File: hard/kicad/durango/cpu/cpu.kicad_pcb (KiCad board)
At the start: 2 copper layers, 34 parts, among them J1 NANOLINK, J2 IO9 INPUT, J3 IO8 PORT, Q1 BC547, Q2 BC547, Q3 BC547, SW1 RESET, U1 65SC02, U10 4040, U11 74HC30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

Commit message: routing in the Mac
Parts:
- moved D1 67.5 mm to (94.0, 78.7)
- moved U8 66.5 mm to (168.9, 121.9), turned to 180 degrees
- moved U6 61.3 mm to (147.3, 104.1)
- moved U10 30.7 mm to (189.2, 104.1)
- moved U11 30.7 mm to (175.3, 106.7)
- moved BZ1 24.3 mm to (188.0, 61.0)
- moved D3 19.9 mm to (182.9, 71.1), turned to 90 degrees
- moved R5 19.3 mm to (186.7, 71.1), turned to 90 degrees
- moved U5 19.1 mm to (193.7, 74.9)
- moved Q3 18.2 mm to (188.0, 49.5), turned to 270 degrees
- moved R4 15.5 mm to (200.7, 62.2), turned to 90 degrees
- moved R3 7.41 mm to (129.5, 116.8), turned to 270 degrees
- moved U4 6.35 mm to (180.3, 74.9)
- moved D2 3.81 mm to (200.7, 49.5), turned to 270 degrees
- moved D4 2.84 mm to (182.9, 59.7), turned to 90 degrees
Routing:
- net /DI7: track 5.08 -> 41.3 mm
- net /DI6: track 5.08 -> 37.8 mm
- net /D4: track 54.8 -> 86.4 mm, vias 2 -> 3
- net /D5: track 74.4 -> 105.2 mm, vias 6 -> 7
- net /D6: track 52.8 -> 82.9 mm, vias 3 -> 4
- net /DI5: track 5.08 -> 34.2 mm
- net /DI0: track 5.08 -> 32.4 mm, vias 0 -> 1
- net /DI1: track 5.08 -> 30.6 mm, vias 0 -> 1
- net /DI4: track 5.08 -> 30.6 mm
- net /DI2: track 5.08 -> 28.8 mm, vias 0 -> 1
- net /IEN: track 0.00 -> 22.6 mm
- net /DI3: track 5.08 -> 27.0 mm, vias 0 -> 1
- net GND: track 11.4 -> 23.4 mm, vias 0 -> 1
- net Net-(C1-Pad1): track 0.00 -> 8.67 mm
- net +5V: track 37.9 -> 45.5 mm

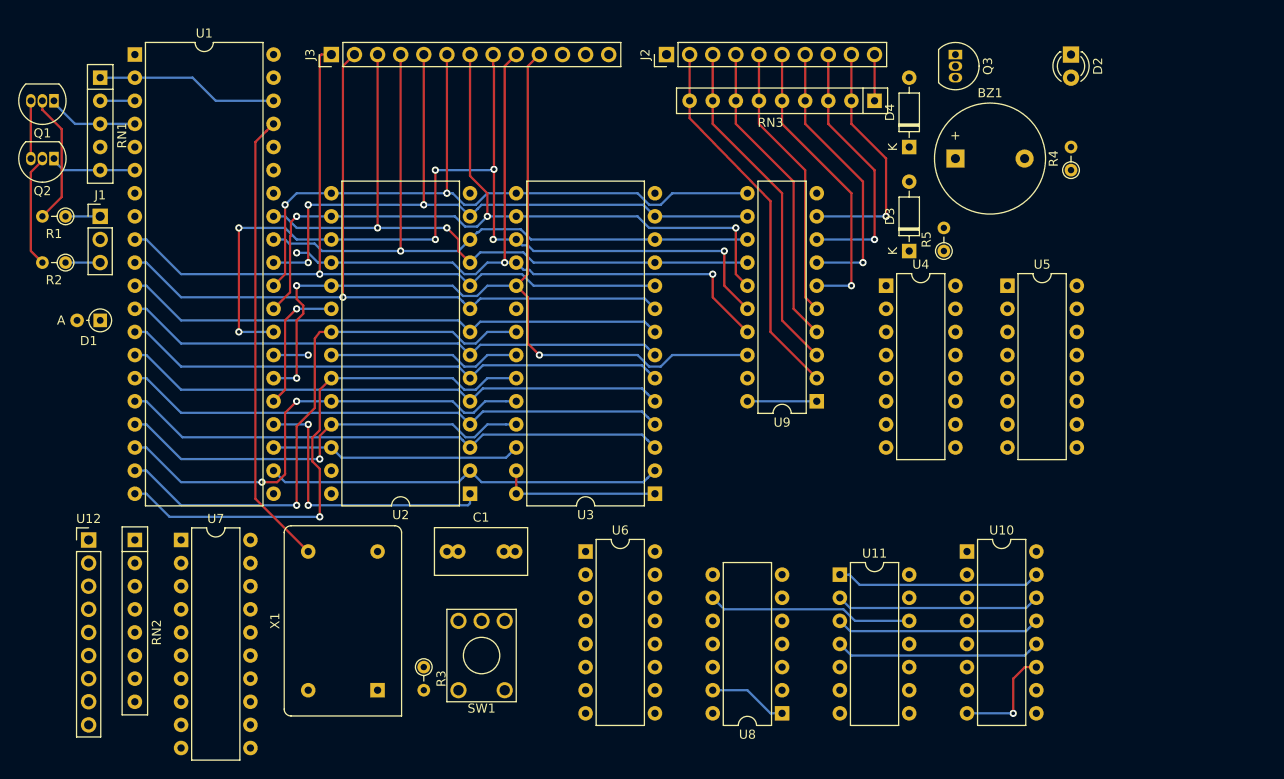
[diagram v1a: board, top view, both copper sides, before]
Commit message: more routing in Raspberry Pi
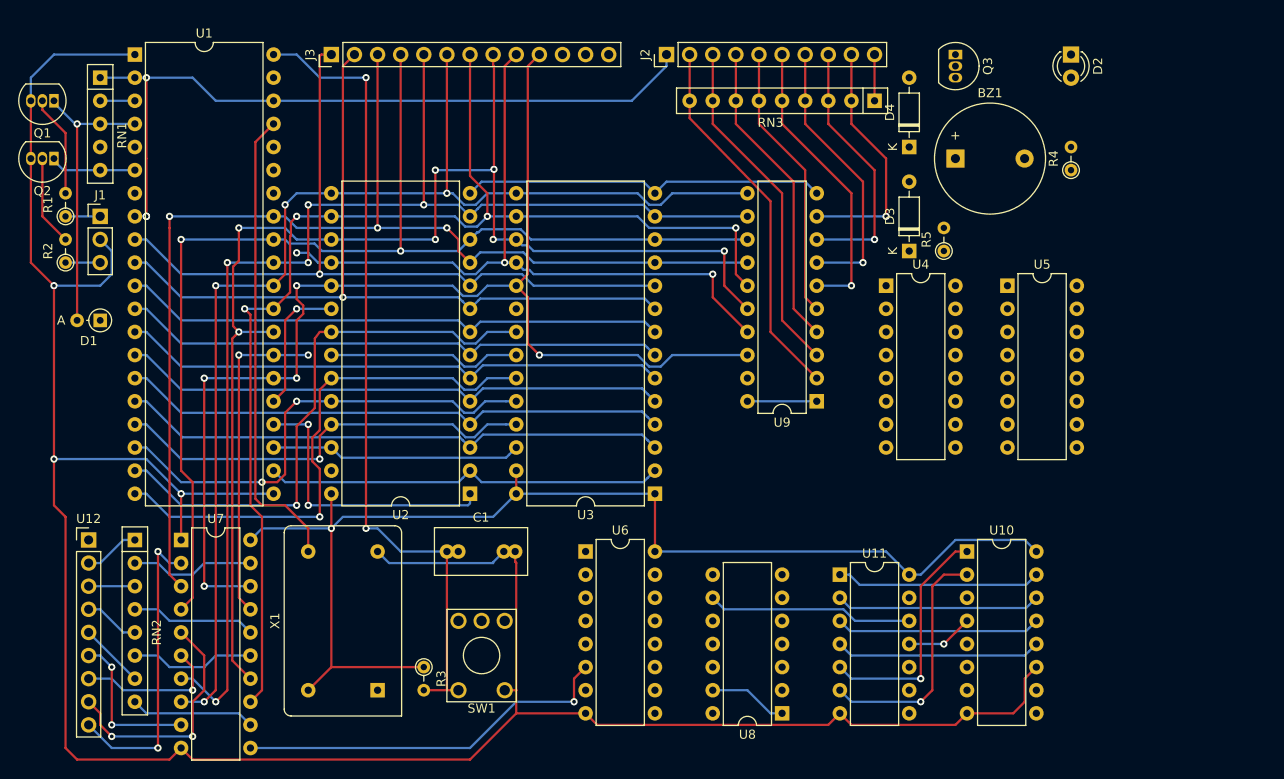
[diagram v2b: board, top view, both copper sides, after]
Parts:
- turned R1 to 90 degrees
- turned R2 to 90 degrees
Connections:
- U11 pad 14: (no net) -> +5V
- U11 pad 7: (no net) -> GND
- U4 pad 16: (no net) -> +5V
- U4 pad 8: (no net) -> GND
- U5 pad 16: (no net) -> +5V
- U5 pad 8: (no net) -> GND
- U6 pad 16: (no net) -> +5V
- U6 pad 8: (no net) -> GND
- U8 pad 14: (no net) -> +5V
- U8 pad 7: (no net) -> GND
- X1 pad 7: Net-(U1-Pad39) -> GND
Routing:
- net GND: track 23.4 -> 325.1 mm, vias 1 -> 3
- net +5V: track 45.5 -> 223.6 mm, vias 0 -> 4
- net Net-(C1-Pad1): track 8.67 -> 98.4 mm, vias 0 -> 2
- net /D2: track 76.5 -> 135.2 mm, vias 3 -> 5
- net /D3: track 78.1 -> 133.2 mm, vias 2 -> 4
- net /D0: track 74.9 -> 127.5 mm, vias 3 -> 4
- net /D1: track 75.6 -> 127.5 mm, vias 1 -> 2
- net /D4: track 86.4 -> 134.0 mm, vias 3 -> 4
- net Net-(U6-Pad6): track 0.00 -> 42.0 mm, vias 0 -> 1
- net /D5: track 105.2 -> 144.9 mm
- net /D7: track 97.4 -> 133.0 mm, vias 3 -> 5
- net Net-(U12-Pad9): track 0.00 -> 33.3 mm, vias 0 -> 2
- net /D6: track 82.9 -> 115.1 mm, vias 4 -> 5
- net Net-(U10-Pad2): track 0.00 -> 27.0 mm, vias 0 -> 1
- net Net-(U12-Pad8): track 0.00 -> 26.8 mm, vias 0 -> 2
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
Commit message: almost routed Durango CPU board
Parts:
- moved D3 8.89 mm to (182.9, 62.2), turned to 270 degrees
- moved R5 5.08 mm to (191.8, 71.1), turned to 0 degrees
- moved U5 0.63 mm to (194.3, 74.9)
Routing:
- net GND: track 325.1 -> 500.8 mm, vias 3 -> 7
- net Net-(U1-Pad39): track 0.00 -> 147.7 mm, vias 0 -> 4
- net Net-(D1-Pad1): track 0.00 -> 123.9 mm, vias 0 -> 3
- net +5V: track 223.6 -> 337.1 mm, vias 4 -> 5
- net Net-(RN1-Pad2): track 3.81 -> 111.2 mm, vias 0 -> 1
- net Net-(U1-Pad34): track 0.00 -> 96.6 mm, vias 0 -> 1
- net Net-(U2-Pad27): track 0.00 -> 92.8 mm, vias 0 -> 3
- net /A13: track 27.6 -> 118.6 mm, vias 0 -> 2
- net /~IO8U: track 0.00 -> 85.7 mm, vias 0 -> 2
- net Net-(U3-Pad20): track 0.00 -> 75.2 mm, vias 0 -> 2
- net /~IO8Q: track 0.00 -> 71.8 mm, vias 0 -> 1
- net Net-(D3-Pad2): track 0.00 -> 56.9 mm, vias 0 -> 2
- net Net-(U2-Pad22): track 21.4 -> 77.6 mm, vias 0 -> 2
- net /A15: track 15.0 -> 57.1 mm
- net Net-(U6-Pad11): track 0.00 -> 40.4 mm, vias 0 -> 1
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
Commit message: finished Durango CPU routing
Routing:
- net /A14: track 54.3 -> 156.4 mm, vias 2 -> 4
- net Net-(R4-Pad1): track 0.00 -> 80.8 mm, vias 0 -> 2
- net /A12: track 44.0 -> 123.1 mm, vias 0 -> 3
- net /A15: track 57.1 -> 132.4 mm, vias 1 -> 4
- net +5V: track 337.1 -> 388.0 mm, vias 5 -> 8
- net /D0: track 127.5 -> 176.8 mm, vias 4 -> 5
- net Net-(U4-Pad7): track 0.00 -> 48.8 mm, vias 0 -> 2
- net /A0: track 85.6 -> 134.2 mm, vias 1 -> 2
- net Net-(U4-Pad6): track 0.00 -> 44.8 mm, vias 0 -> 2
- net /D6: track 115.1 -> 126.9 mm
- net GND: track 500.8 -> 499.5 mm
- net Net-(C1-Pad1): track 129.5 -> 130.7 mm

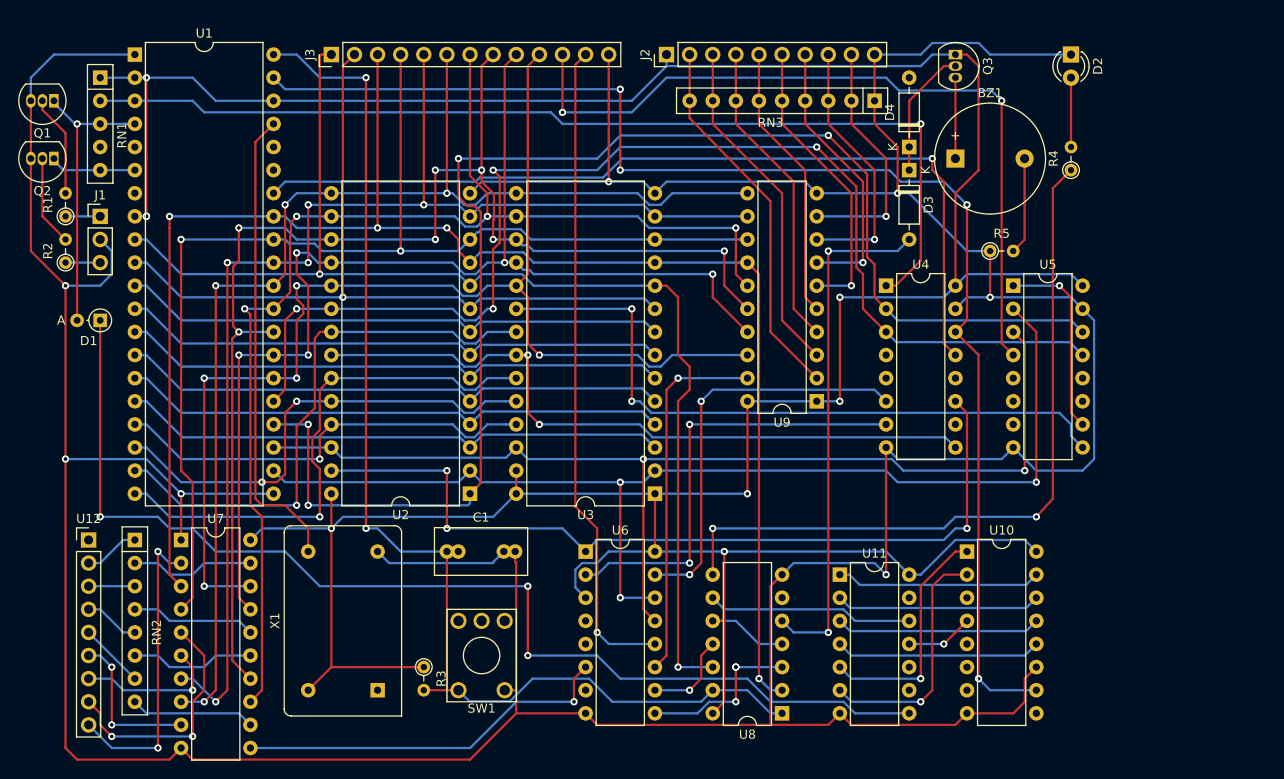
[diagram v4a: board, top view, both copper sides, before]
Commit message: optimised vias and power lines on Durango CPU board
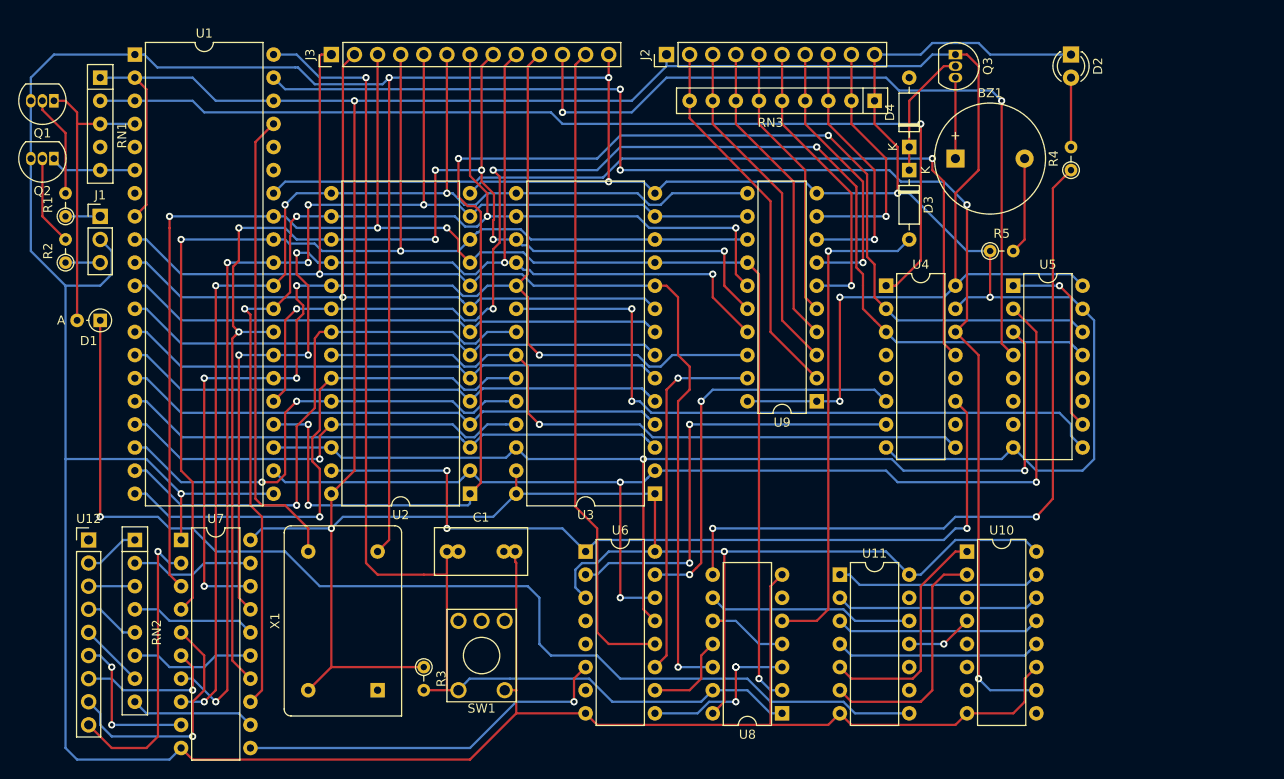
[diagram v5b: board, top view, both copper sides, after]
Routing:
- net GND: track 499.5 -> 564.4 mm, vias 7 -> 6
- net +5V: track 388.0 -> 411.7 mm, vias 8 -> 5
- net Net-(D3-Pad2): track 56.9 -> 54.4 mm, vias 2 -> 1
- net Net-(C1-Pad1): track 130.7 -> 133.0 mm, vias 2 -> 1
- net Net-(D1-Pad1): track 123.9 -> 122.4 mm, vias 3 -> 1
- net Net-(D1-Pad2): track 31.7 -> 32.5 mm, vias 1 -> 0
- net Net-(U2-Pad22): track 77.6 -> 76.8 mm, vias 2 -> 1
- net Net-(U12-Pad9): track 33.3 -> 32.6 mm, vias 2 -> 1
- net Net-(U10-Pad1): track 26.2 -> 25.7 mm, vias 1 -> 0
- net Net-(U10-Pad2): vias 1 -> 0
- net Net-(U6-Pad10): vias 1 -> 0
- net Net-(U12-Pad8): vias 2 -> 1
- net /~IO8Q: vias 1 -> 0
